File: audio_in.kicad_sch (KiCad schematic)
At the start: 26 parts, among them J4 JST SH3, J5 Header_2x1, J6 JST SH3, J7 415-47-208-41-004000, U2 OPA1678

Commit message: Preliminary layout complete, done on airpane so needs verification.
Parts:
- added J10: AudioJack2, Connector_Audio:Jack_3.5mm_PJ320D_Horizontal, symbol Connector_Audio:AudioJack2
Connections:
- net FB_RES: now also J4.1 (Pin_1); no longer J4.3 (Pin_3)
- net FIRST_STAGE_OUT: now also J4.3 (Pin_3); no longer J4.1 (Pin_1)
- net GND: now also U2.9 (EP), J10.S
- net JACK_IN: now also J10.T
- net SECOND_STAGE_P: now reaches R16.2, U2.5 (+)
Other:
- note added: "TODO: Check tip/sleeve"
- note added: "TODO: Pin 9/EPAD on OPA1678"
- moved on the sheet: J4, R10

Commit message: Started adding some 3D models and footprints.
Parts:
- J10: footprint Connector_Audio:Jack_3.5mm_PJ320D_Horizontal -> connectors:CONN_MJ-3523_CUD
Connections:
- net GND: now also J10.1 (S); no longer J10.S
- net JACK_IN: now also J10.2 (T); no longer J10.T
- no-connect marks 0 -> 1
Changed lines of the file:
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@@
 		(color 0 0 0 0)
+	)
+	(no_connect
+		(at 39.37 110.49)
 	)
 	(wire
@@
 	)
 	(symbol
+		(lib_id "Connector_Audio:AudioJack2")
+		(at 30.48 113.03 0)
+		(mirror x)
+		(unit 1)
+		(body_style 1)
+		(exclude_from_sim no)
+		(in_bom yes)
+		(on_board yes)
+		(in_pos_files yes)
+		(dnp no)
+		(property "Reference" "J10"
+			(at 29.845 121.92 0)
+			(show_name no)
+			(do_not_autoplace no)
+			(effects
+				(font
+					(size 1.27 1.27)
+				)
+			)
+		)
+		(property "Value" "AudioJack2"
+			(at 29.845 119.38 0)
+			(show_name no)
+			(do_not_autoplace no)
+			(effects
+				(font
+					(size 1.27 1.27)
+				)
+			)
+		)
+		(property "Footprint" "connectors:CONN_MJ-3523_CUD"
+			(at 31.242 107.442 0)
+			(hide yes)
+			(show_name no)
+			(do_not_autoplace no)
+			(effects
+				(font
+					(size 1.27 1.27)
+				)
+			)
+		)
+		(property "Datasheet" ""
+			(at 30.48 113.03 0)
+			(hide yes)
+			(show_name no)
+			(do_not_autoplace no)
+			(effects
+				(font
+					(size 1.27 1.27)
+				)
+			)
+		)
+		(property "Description" "Audio Jack, 2 Poles (Mono / TS)"
+			(at 29.464 104.648 0)
+			(hide yes)
+			(show_name no)
+			(do_not_autoplace no)
+			(effects
+				(font
+					(size 1.27 1.27)
+				)
+			)
+		)
+		(pin "10"
+		)
+		(pin "2"
+		)
+		(pin "1"
+		)
+		(instances
+			(project "headphone_amp"
+				(path "/62ffec33-ae93-49a8-bfe6-566578dd8e82/fdaed4ad-6382-4025-bc3e-39eb3bc4a0fb"
+					(reference "J10")
+					(unit 1)
+				)
+			)
+		)
+	)
+	(symbol
 		(lib_id "#inventree_kicad:R_51K_0402_1PCT_0W0625")
 		(at 124.46 128.27 90)
@@
 					(unit 1)
 				)
-			)
-		)
-	)
-	(symbol
-		(lib_id "Connector_Audio:AudioJack2")
-		(at 34.29 113.03 0)
-		(mirror x)
-		(unit 1)
-		(body_style 1)
-		(exclude_from_sim no)
-		(in_bom yes)
-		(on_board yes)
-		(in_pos_files yes)
-		(dnp no)
-		(property "Reference" "J10"
-			(at 33.655 121.92 0)
-			(show_name no)
-			(do_not_autoplace no)
-			(effects
-				(font
-					(size 1.27 1.27)
-				)
-			)
-		)
-		(property "Value" "AudioJack2"
-			(at 33.655 119.38 0)
-			(show_name no)
-			(do_not_autoplace no)
-			(effects
-				(font
-					(size 1.27 1.27)
-				)
-			)
-		)
-		(property "Footprint" "Connector_Audio:Jack_3.5mm_PJ320D_Horizontal"
-			(at 34.29 113.03 0)
-			(hide yes)
-			(show_name no)
-			(do_not_autoplace no)
-			(effects
-				(font
-					(size 1.27 1.27)
-				)
-			)
-		)
-		(property "Datasheet" ""
-			(at 34.29 113.03 0)
-			(hide yes)
-			(show_name no)
-			(do_not_autoplace no)
-			(effects
-				(font
-					(size 1.27 1.27)
-				)
-			)
-		)
-		(property "Description" "Audio Jack, 2 Poles (Mono / TS)"
-			(at 34.29 113.03 0)
-			(hide yes)
-			(show_name no)
-			(do_not_autoplace no)
-			(effects
-				(font
-					(size 1.27 1.27)
-				)
-			)
-		)
-		(pin "S"
-		)
-		(pin "T"
-		)
-		(instances
-			(project "headphone_amp"
-				(path "/62ffec33-ae93-49a8-bfe6-566578dd8e82/fdaed4ad-6382-4025-bc3e-39eb3bc4a0fb"
-					(reference "J10")
-					(unit 1)
-				)

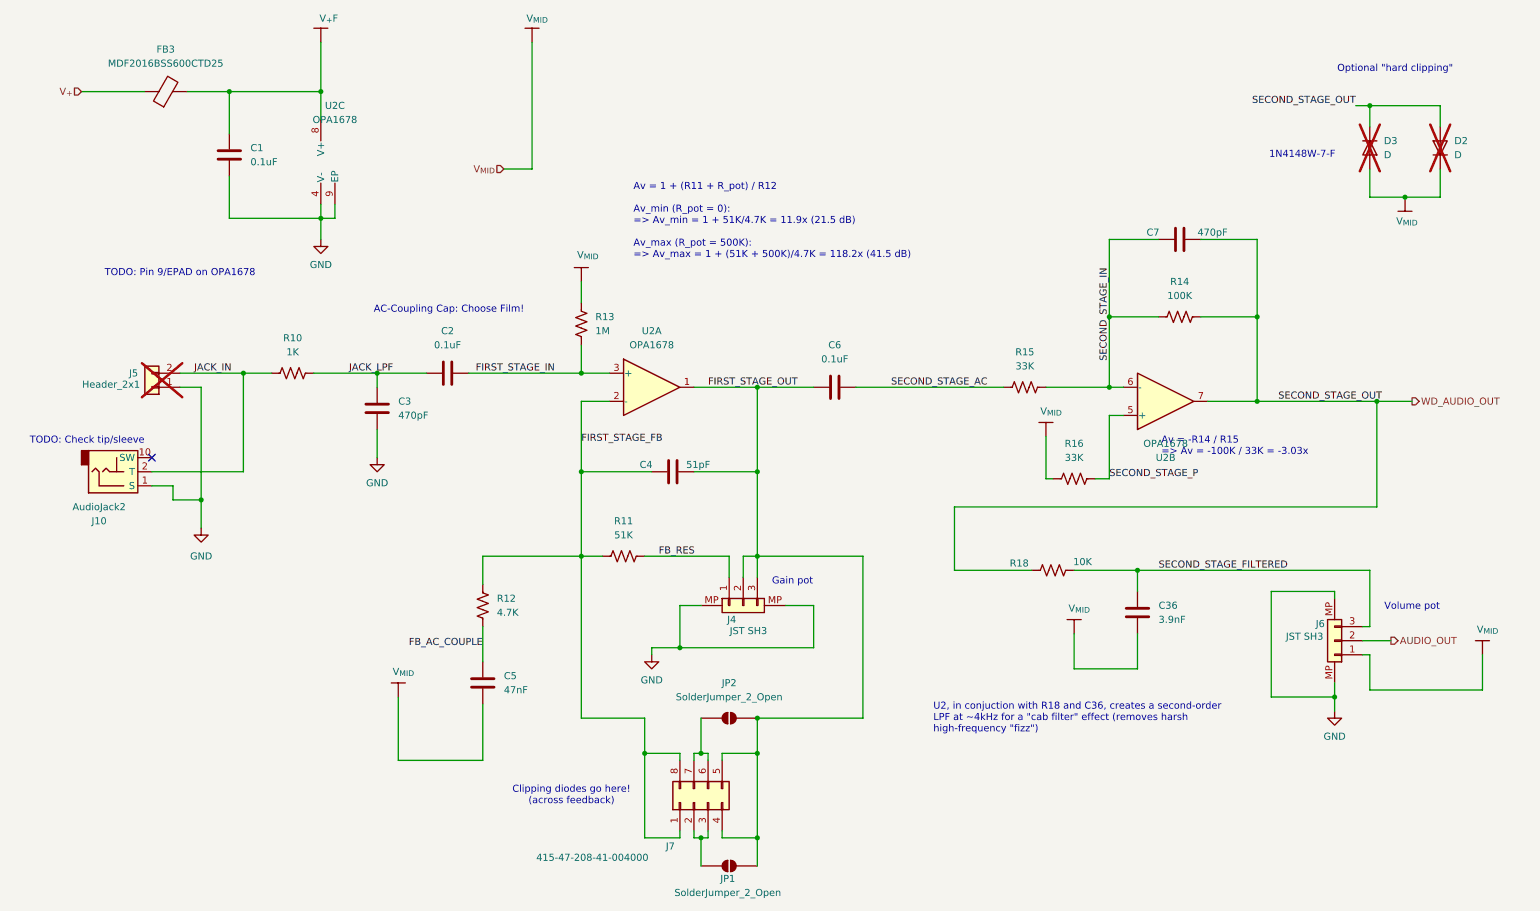
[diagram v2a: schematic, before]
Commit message: Picked off the board parts and ordered on DigiKey -- also added notes on schematic.
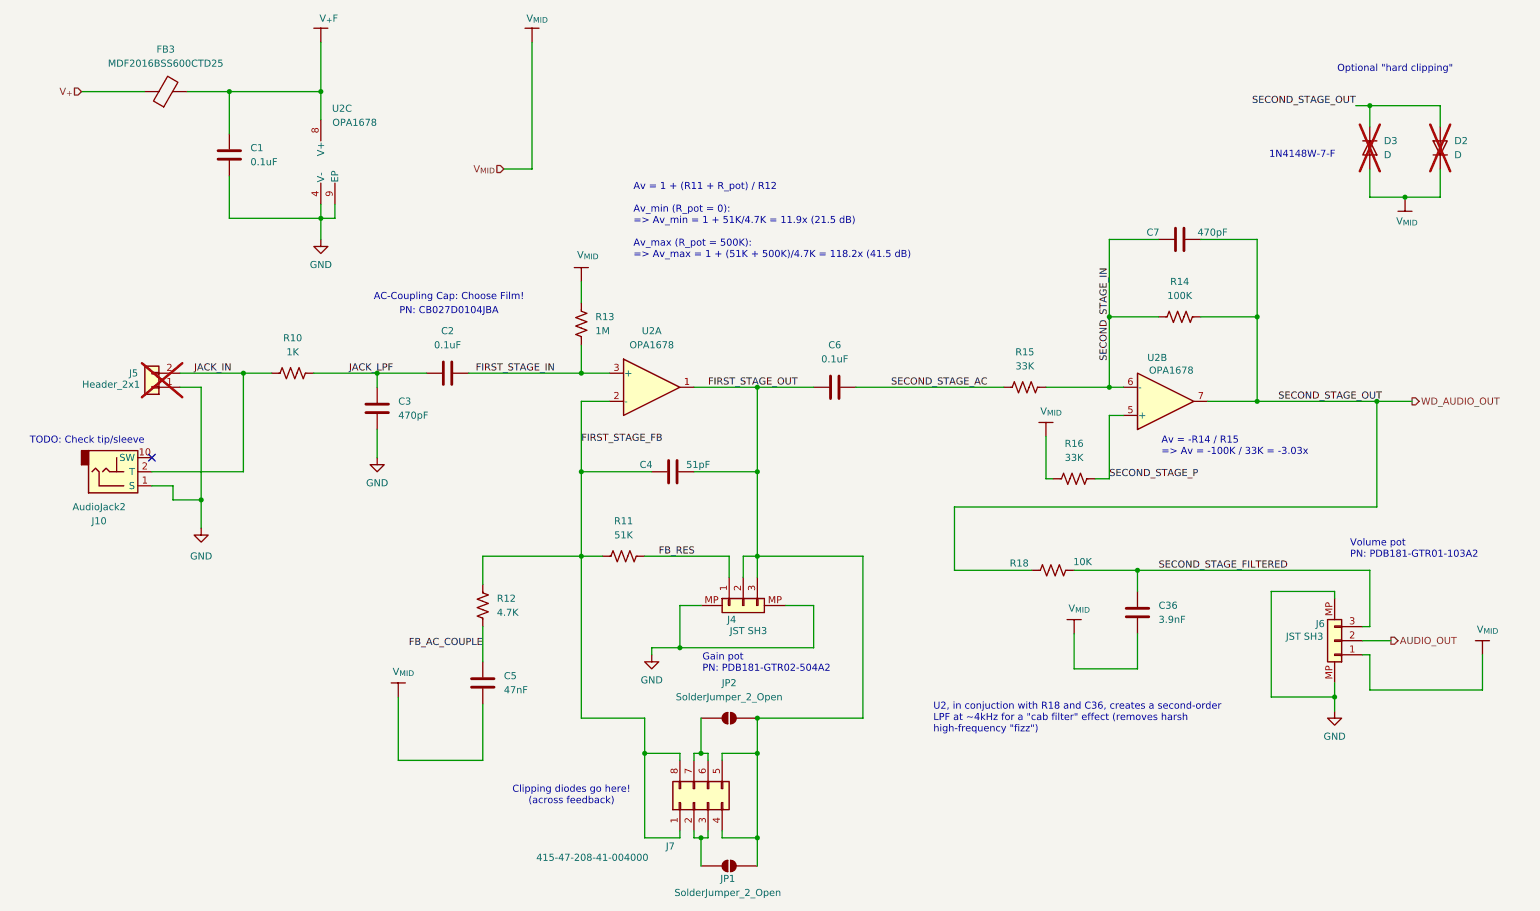
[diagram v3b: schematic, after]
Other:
- note added: "Gain pot PN: PDB181-GTR02-504A2"
- note added: "PN: CB027D0104JBA"
- note added: "Volume pot PN: PDB181-GTR01-103A2"
- note removed: "Gain pot"
- note removed: "TODO: Pin 9/EPAD on OPA1678"
- note removed: "Volume pot"
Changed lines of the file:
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@@
 		(comment 1 "${PCBA_IPN}")
 	)
-	(text "Optional \"hard clipping\""
+	(text "PN: CB027D0104JBA "
 		(exclude_from_sim no)
-		(at 263.652 40.386 0)
+		(at 92.964 84.074 0)
 		(effects
 			(font
@@
 		)
 	)
-	(text "TODO: Pin 9/EPAD on OPA1678"
+	(text "Optional \"hard clipping\""
 		(exclude_from_sim no)
-		(at 44.45 77.216 0)
+		(at 263.652 40.386 0)
 		(effects
 			(font
@@
 		)
 	)
-	(text "Volume pot"
+	(text "Gain pot\nPN: PDB181-GTR02-504A2"
 		(exclude_from_sim no)
-		(at 266.7 137.414 0)
+		(at 138.684 147.574 0)
 		(effects
 			(font
 				(size 1.27 1.27)
 			)
+			(justify left)
 		)
 	)
-	(text "AC-Coupling Cap: Choose Film!"
+	(text "Volume pot\nPN: PDB181-GTR01-103A2"
 		(exclude_from_sim no)
-		(at 92.964 83.82 0)
+		(at 255.524 127 0)
 		(effects
 			(font
 				(size 1.27 1.27)
 			)
+			(justify left)
 		)
 	)
-	(text "Clipping diodes go here!\n(across feedback)"
+	(text "AC-Coupling Cap: Choose Film!"
 		(exclude_from_sim no)
-		(at 115.062 171.45 0)
+		(at 92.964 81.534 0)
 		(effects
 			(font
@@
 		)
 	)
-	(text "Gain pot"
+	(text "Clipping diodes go here!\n(across feedback)"
 		(exclude_from_sim no)
-		(at 154.94 132.842 0)
+		(at 115.062 171.45 0)
 		(effects
 			(font
@@
 		(in_pos_files yes)
 		(dnp no)
-		(fields_autoplaced yes)
 		(property "Reference" "U2"
-			(at 72.39 46.99 0)
+			(at 73.66 47.498 0)
 			(show_name no)
 			(do_not_autoplace no)
@@
 		)
 		(property "Value" "OPA1678"
-			(at 72.39 49.53 0)
+			(at 75.946 50.038 0)
 			(show_name no)
 			(do_not_autoplace no)
@@
 		(dnp no)
 		(property "Reference" "U2"
-			(at 222.25 110.49 0)
+			(at 220.726 92.456 0)
 			(show_name no)
 			(do_not_autoplace no)
@@
 		)
 		(property "Value" "OPA1678"
-			(at 222.25 107.95 0)
+			(at 223.266 94.742 0)
 			(show_name no)
 			(do_not_autoplace no)

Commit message: Finilizing DRC and ERC
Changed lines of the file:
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@@
 	)
 	(junction
+		(at 60.96 44.45)
+		(diameter 0)
+		(color 0 0 0 0)
+	)
+	(junction
 		(at 148.59 179.07)
 		(diameter 0)
@@
 	(wire
 		(pts
+			(xy 60.96 44.45) (xy 69.85 44.45)
+		)
+		(stroke
+			(width 0)
+			(type default)
+		)
+	)
+	(wire
+		(pts
 			(xy 279.4 152.4) (xy 279.4 146.05)
 		)
@@
 	(wire
 		(pts
+			(xy 60.96 41.91) (xy 60.96 44.45)
+		)
+		(stroke
+			(width 0)
+			(type default)
+		)
+	)
+	(wire
+		(pts
 			(xy 209.55 114.3) (xy 212.09 114.3)
 		)
@@
 	(wire
 		(pts
-			(xy 53.34 44.45) (xy 69.85 44.45)
+			(xy 53.34 44.45) (xy 60.96 44.45)
 		)
 		(stroke
@@
 					(unit 1)
 				)
+			)
+		)
+	)
+	(symbol
+		(lib_id "power:PWR_FLAG")
+		(at 60.96 41.91 0)
+		(unit 1)
+		(body_style 1)
+		(exclude_from_sim no)
+		(in_bom yes)
+		(on_board yes)
+		(in_pos_files yes)
+		(dnp no)
+		(fields_autoplaced yes)
+		(property "Reference" "#FLG06"
+			(at 60.96 40.005 0)
+			(hide yes)
+			(show_name no)
+			(do_not_autoplace no)
+			(effects
+				(font
+					(size 1.27 1.27)
+				)
+			)
+		)
+		(property "Value" "PWR_FLAG"
+			(at 60.96 36.83 0)
+			(show_name no)
+			(do_not_autoplace no)
+			(effects
+				(font
+					(size 1.27 1.27)
+				)
+			)
+		)
+		(property "Footprint" ""
+			(at 60.96 41.91 0)
+			(hide yes)
+			(show_name no)
+			(do_not_autoplace no)
+			(effects
+				(font
+					(size 1.27 1.27)
+				)
+			)
+		)
+		(property "Datasheet" ""
+			(at 60.96 41.91 0)
+			(hide yes)
+			(show_name no)
+			(do_not_autoplace no)
+			(effects
+				(font
+					(size 1.27 1.27)
+				)
+			)
+		)
+		(property "Description" "Special symbol for telling ERC where power comes from"
+			(at 60.96 41.91 0)
+			(hide yes)
+			(show_name no)
+			(do_not_autoplace no)
+			(effects
+				(font
+					(size 1.27 1.27)
+				)
+			)
+		)
+		(pin "1"
+		)
+		(instances
+			(project "headphone_amp"
+				(path "/62ffec33-ae93-49a8-bfe6-566578dd8e82/fdaed4ad-6382-4025-bc3e-39eb3bc4a0fb"
+					(reference "#FLG06")
+					(unit 1)
+				)

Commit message: Finally updated all parts in InvenTree and linked them with KiCAD. Ready for BOM exports to JLC.
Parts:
- C1: symbol #inventree_kicad:C_0U1_X7R_16V_0402 -> inventree_kicad:C_0U1_X7R_25V_0402; IPN 301-0003 -> 301-0018; InvenTree 16 -> 52; Part URL http://10.0.0.33/web/part/16/ -> http://10.0.0.33/web/part/52/
- D2, D3: value D -> 1N4148W; symbol Device:D -> inventree_kicad:D_SWITCHING_100V_300MA_SOD123; IPN (none) -> 308-0002; InvenTree (none) -> 37; Part URL (none) -> http://10.0.0.33/web/part/37/
- FB3: value MDF2016BSS600CTD25 -> 60R @ 2MHz; symbol Device:FerriteBead -> inventree_kicad:FB_60R_0806_0A85; IPN (none) -> 306-0003; InvenTree (none) -> 60; Part URL (none) -> http://10.0.0.33/web/part/60/
- J10: value AudioJack2 -> MJ-3523-SMT-TR; symbol Connector_Audio:AudioJack2 -> inventree_kicad:AUDIO_JACK_3.5MM_MJ-3523-SMT; IPN (none) -> 310-0008; InvenTree (none) -> 40; Part URL (none) -> http://10.0.0.33/web/part/40/
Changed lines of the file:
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@@
 	)
 	(symbol
-		(lib_id "Device:FerriteBead")
+		(lib_id "inventree_kicad:FB_60R_0806_0A85")
 		(at 41.91 44.45 90)
 		(unit 1)
@@
 			)
 		)
-		(property "Value" "MDF2016BSS600CTD25"
+		(property "Value" "60R @ 2MHz"
 			(at 41.8592 39.37 90)
 			(show_name no)
@@
 			)
 		)
-		(property "Description" "Ferrite bead"
+		(property "Description" "60 Ohms @ 2 MHz Power Line Ferrite Bead 0806 (2016 Metric) 850mA 330mOhm"
+			(at 41.91 44.45 0)
+			(hide yes)
+			(show_name no)
+			(do_not_autoplace no)
+			(effects
+				(font
+					(size 1.27 1.27)
+				)
+			)
+		)
+		(property "InvenTree" "60"
+			(at 41.91 44.45 0)
+			(hide yes)
+			(show_name no)
+			(do_not_autoplace no)
+			(effects
+				(font
+					(size 1.27 1.27)
+				)
+			)
+		)
+		(property "Part URL" "http://10.0.0.33/web/part/60/"
+			(at 41.91 44.45 0)
+			(hide yes)
+			(show_name no)
+			(do_not_autoplace no)
+			(effects
+				(font
+					(size 1.27 1.27)
+				)
+			)
+		)
+		(property "IPN" "306-0003"
 			(at 41.91 44.45 0)
 			(hide yes)
@@
 	)
 	(symbol
-		(lib_id "Connector_Audio:AudioJack2")
+		(lib_id "inventree_kicad:AUDIO_JACK_3.5MM_MJ-3523-SMT")
 		(at 30.48 113.03 0)
 		(mirror x)
@@
 			)
 		)
-		(property "Value" "AudioJack2"
+		(property "Value" "MJ-3523-SMT-TR"
 			(at 29.845 119.38 0)
 			(show_name no)
@@
 			)
 		)
-		(property "Description" "Audio Jack, 2 Poles (Mono / TS)"
+		(property "Description" "3.5 mm Audio Jack, Surface Mount, Right Angle"
 			(at 29.464 104.648 0)
+			(hide yes)
+			(show_name no)
+			(do_not_autoplace no)
+			(effects
+				(font
+					(size 1.27 1.27)
+				)
+			)
+		)
+		(property "InvenTree" "40"
+			(at 30.48 113.03 0)
+			(hide yes)
+			(show_name no)
+			(do_not_autoplace no)
+			(effects
+				(font
+					(size 1.27 1.27)
+				)
+			)
+		)
+		(property "Part URL" "http://10.0.0.33/web/part/40/"
+			(at 30.48 113.03 0)
+			(hide yes)
+			(show_name no)
+			(do_not_autoplace no)
+			(effects
+				(font
+					(size 1.27 1.27)
+				)
+			)
+		)
+		(property "IPN" "310-0008"
+			(at 30.48 113.03 0)
 			(hide yes)
 			(show_name no)
@@
 	)
 	(symbol
-		(lib_id "Device:D")
+		(lib_id "inventree_kicad:D_SWITCHING_100V_300MA_SOD123")
 		(at 271.78 54.61 90)
 		(unit 1)
@@
 			)
 		)
-		(property "Value" "D"
+		(property "Value" "1N4148W"
 			(at 274.32 55.8799 90)
 			(show_name no)
@@
 			)
 		)
-		(property "Description" "Diode"
+		(property "Description" "Diode Standard 100 V 300mA Surface Mount SOD-123"
 			(at 271.78 54.61 0)
 			(hide yes)
@@
 		)
 		(property "Sim.Pins" "1=K 2=A"
+			(at 271.78 54.61 0)
+			(hide yes)
+			(show_name no)
+			(do_not_autoplace no)
+			(effects
+				(font
+					(size 1.27 1.27)
+				)
+			)
+		)
+		(property "InvenTree" "37"
+			(at 271.78 54.61 0)
+			(hide yes)
+			(show_name no)
+			(do_not_autoplace no)
+			(effects
+				(font
+					(size 1.27 1.27)
+				)
+			)
+		)
+		(property "Part URL" "http://10.0.0.33/web/part/37/"
+			(at 271.78 54.61 0)
+			(hide yes)
+			(show_name no)
+			(do_not_autoplace no)
+			(effects
+				(font
+					(size 1.27 1.27)
+				)
+			)
+		)
+		(property "IPN" "308-0002"
 			(at 271.78 54.61 0)
 			(hide yes)
@@
 	)
 	(symbol
-		(lib_id "Device:D")
+		(lib_id "inventree_kicad:D_SWITCHING_100V_300MA_SOD123")
 		(at 259.08 54.61 270)
 		(unit 1)
@@
 			)
 		)
-		(property "Value" "D"
+		(property "Value" "1N4148W"
 			(at 261.62 55.8799 90)
 			(show_name no)
@@
 			)
 		)
-		(property "Description" "Diode"
+		(property "Description" "Diode Standard 100 V 300mA Surface Mount SOD-123"
 			(at 259.08 54.61 0)
 			(hide yes)
@@
 		)
 		(property "Sim.Pins" "1=K 2=A"
+			(at 259.08 54.61 0)
+			(hide yes)
+			(show_name no)
+			(do_not_autoplace no)
+			(effects
+				(font
+					(size 1.27 1.27)
+				)
+			)
+		)
+		(property "InvenTree" "37"
+			(at 259.08 54.61 0)
+			(hide yes)
+			(show_name no)
+			(do_not_autoplace no)
+			(effects
+				(font
+					(size 1.27 1.27)
+				)
+			)
+		)
+		(property "Part URL" "http://10.0.0.33/web/part/37/"
+			(at 259.08 54.61 0)
+			(hide yes)
+			(show_name no)
+			(do_not_autoplace no)
+			(effects
+				(font
+					(size 1.27 1.27)
+				)
+			)
+		)
+		(property "IPN" "308-0002"
 			(at 259.08 54.61 0)
 			(hide yes)
@@
 	)
 	(symbol
-		(lib_id "#inventree_kicad:C_0U1_X7R_16V_0402")
+		(lib_id "inventree_kicad:C_0U1_X7R_25V_0402")
 		(at 53.34 55.88 0)
 		(unit 1)
@@
 			)
 		)
-		(property "Description" "0.1 µF ±10% 16V Ceramic Capacitor X7R 0402 (1005 Metric)"
+		(property "Description" "0.1 µF ±10% 25V Ceramic Capacitor X7R 0402 (1005 Metric)"
 			(at 53.34 55.88 0)
 			(hide yes)
@@
 			)
 		)
-		(property "IPN" "301-0003"
+		(property "IPN" "301-0018"
 			(at 53.34 55.88 0)
 			(hide yes)
@@
 			)
 		)
-		(property "InvenTree" "16"
+		(property "InvenTree" "52"
 			(at 53.34 55.88 0)
 			(hide yes)
@@
 			)
 		)
-		(property "Part URL" "http://10.0.0.33/web/part/16/"
+		(property "Part URL" "http://10.0.0.33/web/part/52/"
 			(at 53.34 55.88 0)
 			(hide yes)
